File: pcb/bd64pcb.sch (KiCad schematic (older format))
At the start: 15 parts

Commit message: switch matrix & usbc prep
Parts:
- added D? (x64): SOD123, symbol Device:D_Small
- added F?: 500mA, symbol Device:Polyfuse_Small
- added J?: USB_C_Receptacle, symbol Connector:USB_C_Receptacle
- added MX? (x64): MX-NoLED, symbol MX_Alps_Hybrid:MX-NoLED
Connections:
- net labels added: VCC, col0, row0
- wire segments 43 -> 242
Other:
- moved on the sheet: C?, R?, SW?, U?, Y?

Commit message: mcp expander
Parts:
- removed D? (x24): SOD123, symbol Device:D_Small
- removed F?: 500mA, symbol Device:Polyfuse_Small
- removed J?: USB_C_Receptacle, symbol Connector:USB_C_Receptacle
- removed MX? (x24): MX-NoLED, symbol MX_Alps_Hybrid:MX-NoLED
- added C? (x4): 0.47uF, symbol Device:C_Small
- added C?: 22uF, symbol Device:CP1_Small
- added C? (x3): 0.1uF, symbol Device:C_Small
- added C?: 1uF, symbol Device:C_Small
- added D? (x25): SOD123, symbol Device:D_Small
- added F?: 500mA, symbol Device:Polyfuse_Small
- added J?: USB_C_Receptacle_USB2.0, symbol Connector:USB_C_Receptacle_USB2.0
- added JP? (x4): SolderJumper_2_Bridged, symbol Jumper:SolderJumper_2_Bridged
- added JP? (x5): SolderJumper_3_Bridged12, symbol Jumper:SolderJumper_3_Bridged12
- added MX? (x25): MX-NoLED, symbol MX_Alps_Hybrid:MX-NoLED
- added R?: 20k, symbol Device:R_Small
- added R? (x2): 5.1k, symbol Device:R_Small
- added R? (x2): 100k, symbol Device:R_Small
- added TP?: TestPoint, symbol Connector:TestPoint
- added U? (x64): QBLP677R-RGB, RGB-REVERSE_MOUNT, symbol QBLP677R-RGB:QBLP677R-RGB
- added U?: MCP23017_SO, Package_SO:SOIC-28W_7.5x17.9mm_P1.27mm, symbol Interface_Expansion:MCP23017_SO
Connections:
- net labels added: CS1, CS10, CS11, CS12, CS13, CS14, CS15, CS16, CS2, CS3, CS4, CS5, CS6, CS7, CS8, CS9, IICRST, INTB, SCL, SDA, SDB, SW1, SW10, SW11, SW12, SW2, SW3, SW4, SW5, SW6, SW7, SW8, SW9, col1, col10, col11, col12, col2, col3, col4, col5, col6, col7, col8, col9, row1, row2, row3, row4
- wire segments 242 -> 968
- no-connect marks 0 -> 8
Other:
- moved on the sheet: C?, D?, MX?, R?, SW?, U?, Y?

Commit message: numbering components
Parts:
- added F2: 500mA, symbol Device:Polyfuse_Small
- added J2: USB_B_Micro, symbol Connector:USB_B_Micro
- added R5, R6, R7: 4.7k, symbol Device:R_Small
- gave numbers to parts that had none: 236
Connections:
- net +5V: now also F2.1, R5.2, R6.2, R7.2
- net D+: now also J2.3 (D+)
- net D-: now also J2.2 (D-)
- net GND: now also J2.5 (GND), J2.6 (Shield)
- net IICRST: now also U1.29 (PB5)
- net INTB: now also U1.20 (PD2), R5.1
- net SCL: now also U1.19 (PD1), R6.1
- net SDA: now also U1.18 (PD0), R7.1
- net SDB: now also U1.31 (PC6)
- net VCC: now also F2.2, J2.1 (VBUS)
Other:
- moved on the sheet: C1, C10, C11, C12, C13, C14, C15, C16, C2, C3, C4, C5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

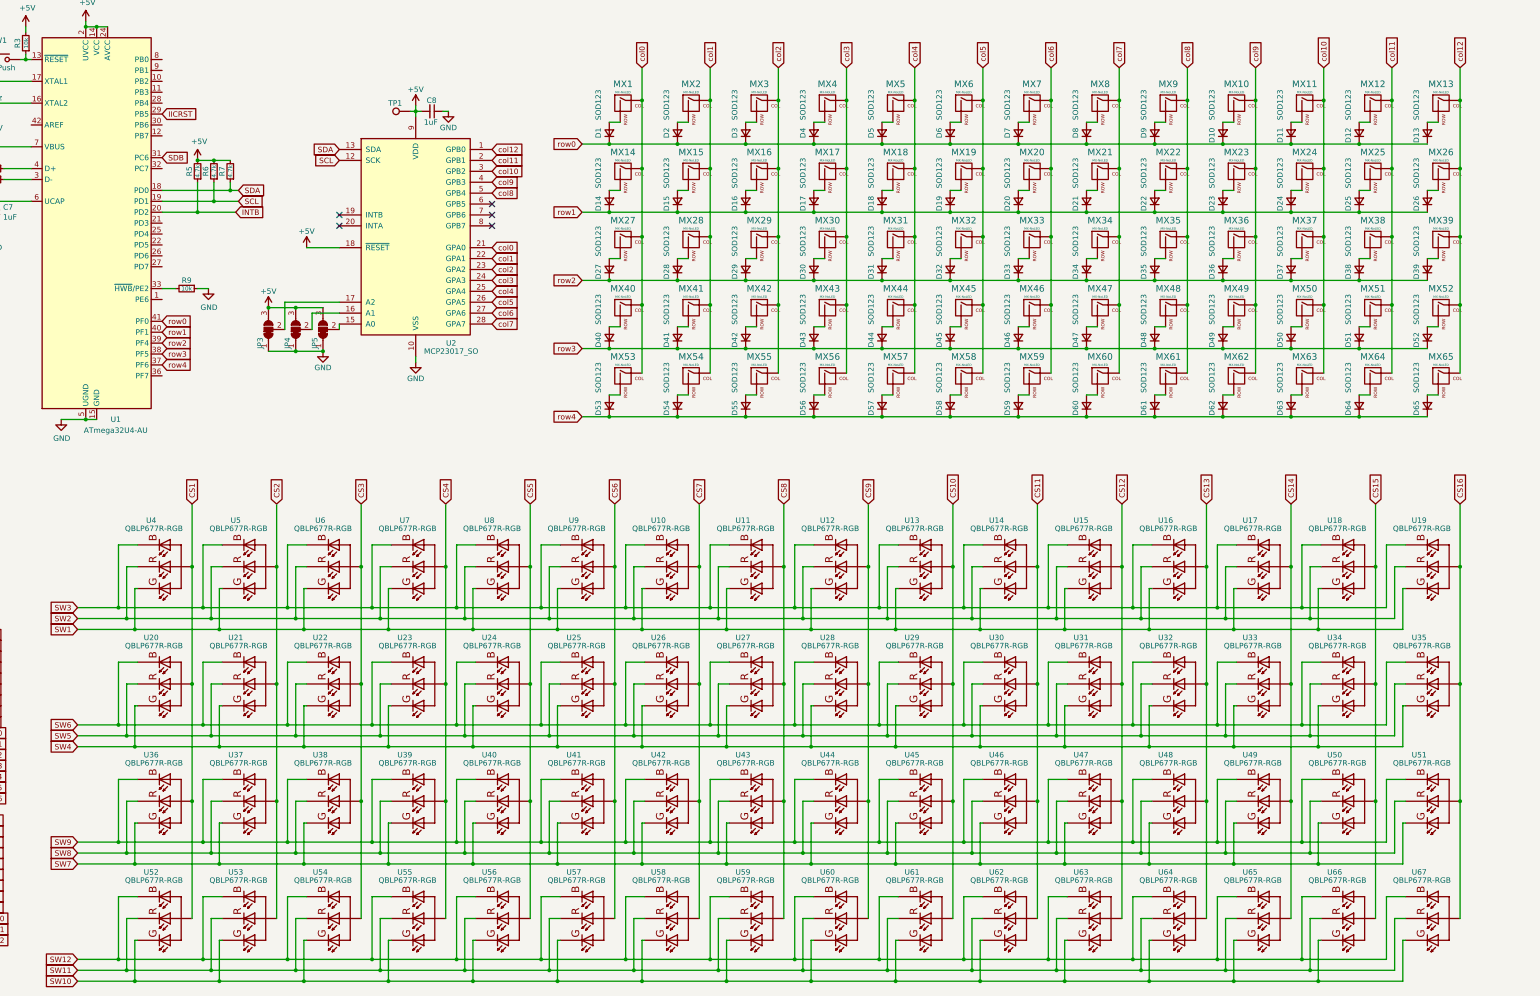
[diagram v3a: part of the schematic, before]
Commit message: assigning footprints
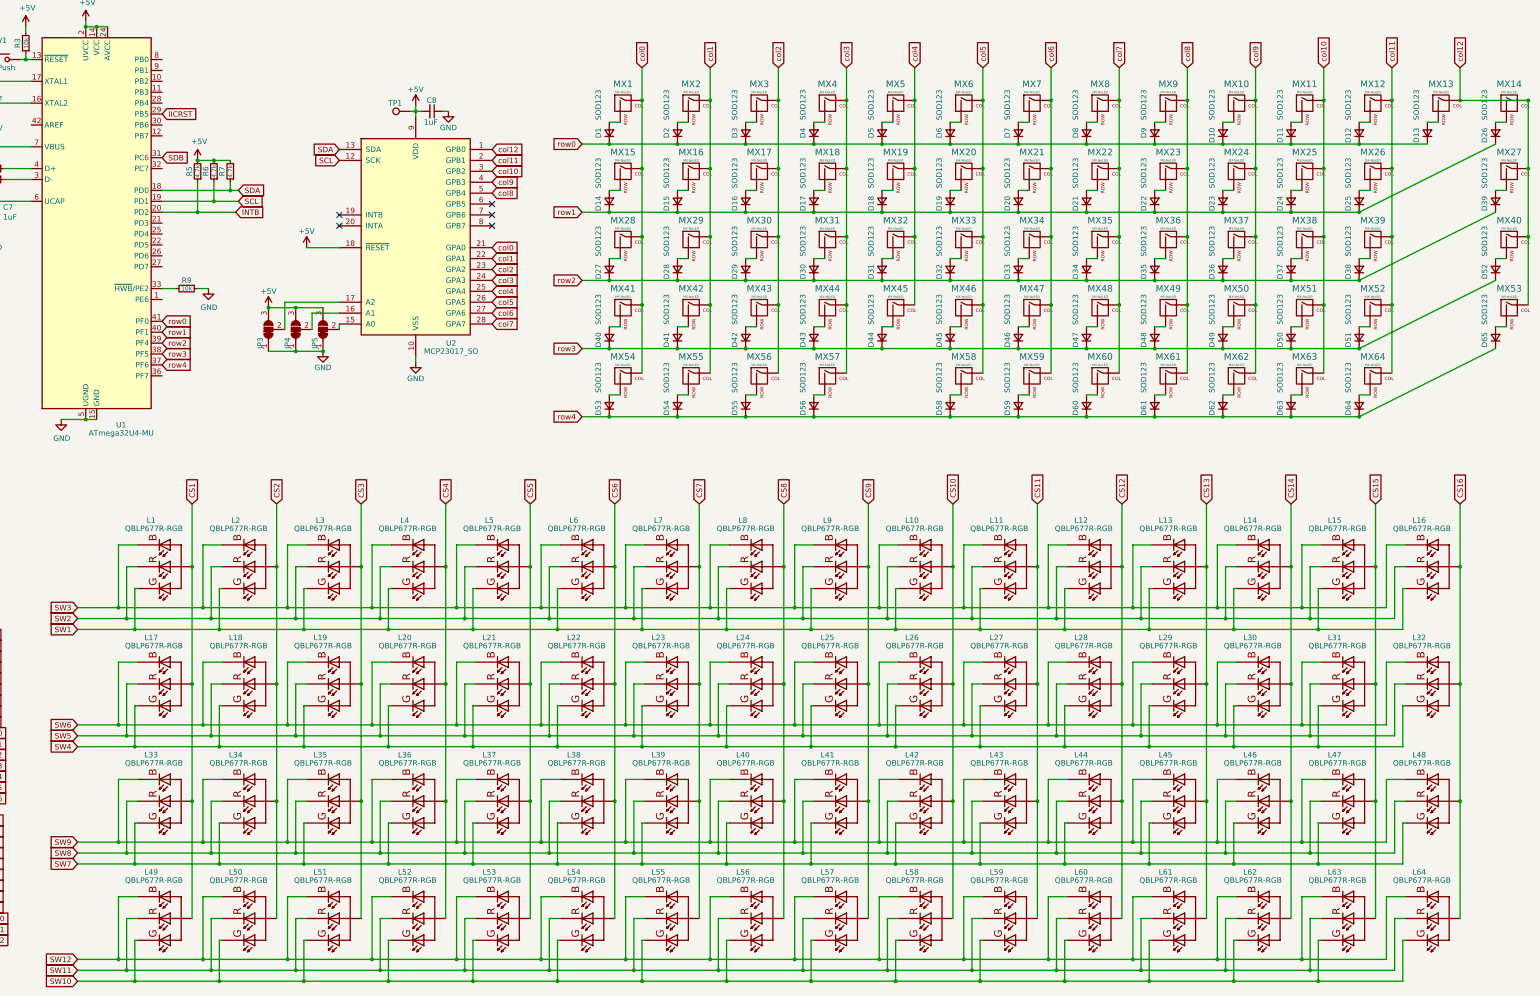
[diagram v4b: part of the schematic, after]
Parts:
- removed D57: SOD123, symbol Device:D_Small
- removed MX57: MX-NoLED, symbol MX_Alps_Hybrid:MX-NoLED
- removed U1: ATmega32U4-AU, Package_QFP:TQFP-44_10x10mm_P0.8mm, symbol MCU_Microchip_ATmega:ATmega32U4-AU
- removed U10, U11, U12, U13, U14, U15, U16, U17, U18, U19, U22, U23, U24, U25, U26, U27, U28, U29, U30, U31, U32, U33, U34, U35, U36, U37, U38, U39, U40, U41, U42, U43, U44, U45, U46, U47, U48, U49, U50, U51, U52, U53, U54, U55, U56, U57, U58, U59, U6, U60, U61, U62, U63, U64, U65, U66, U67, U7, U8, U9: QBLP677R-RGB, RGB-REVERSE_MOUNT, symbol QBLP677R-RGB:QBLP677R-RGB
- added L10, L11, L12, L13, L14, L15, L16, L19, L20, L21, L22, L23, L24, L25, L26, L27, L28, L29, L3, L30, L31, L32, L33, L34, L35, L36, L37, L38, L39, L4, L40, L41, L42, L43, L44, L45, L46, L47, L48, L49, L5, L50, L51, L52, L53, L54, L55, L56, L57, L58, L59, L6, L60, L61, L62, L63, L64, L7, L8, L9: QBLP677R-RGB, QBLP677R-RGB:RGB-REVERSE_MOUNT, symbol QBLP677R-RGB:QBLP677R-RGB
- added U1: ATmega32U4-MU, Package_DFN_QFN:QFN-44-1EP_7x7mm_P0.5mm_EP5.2x5.2mm, symbol MCU_Microchip_ATmega:ATmega32U4-MU
- C1, C10, C11, C12, C13, C14, C15, C16, C2, C3, C4, C5, C6, C7, C8, C9: footprint (none) -> Capacitor_SMD:C_0805_2012Metric
- D1, D10, D11, D12, D13, D14, D15, D16, D17, D18, D19, D2, D20, D21, D22, D23, D24, D25, D26, D27, D28, D29, D3, D30, D31, D32, D33, D34, D35, D36, D37, D38, D39, D4, D40, D41, D42, D43, D44, D45, D46, D47, D48, D49, D5, D50, D51, D52, D53, D54, D55, D56, D58, D59, D6, D60, D61, D62, D63, D64, D65, D7, D8, D9: footprint (none) -> Diode_SMD:D_SOD-123
- F1, F2: footprint (none) -> Fuse:Fuse_1206_3216Metric
- J2: footprint (none) -> random-keyboard-parts:Molex-0548190589
- L1: renamed from U4; footprint RGB-REVERSE_MOUNT -> QBLP677R-RGB:RGB-REVERSE_MOUNT
- L17: renamed from U20; footprint RGB-REVERSE_MOUNT -> QBLP677R-RGB:RGB-REVERSE_MOUNT
- L18: renamed from U21; footprint RGB-REVERSE_MOUNT -> QBLP677R-RGB:RGB-REVERSE_MOUNT
- L2: renamed from U5; footprint RGB-REVERSE_MOUNT -> QBLP677R-RGB:RGB-REVERSE_MOUNT
- MX1, MX10, MX11, MX12, MX13, MX2, MX3, MX4, MX5, MX58, MX59, MX6, MX7, MX8, MX9: footprint (none) -> MX_Alps_Hybrid:MX-1U-NoLED
- MX14: renamed from MX26; footprint (none) -> MX_Alps_Hybrid:MX-1U-NoLED
- MX15: renamed from MX14; footprint (none) -> MX_Alps_Hybrid:MX-1.25U-NoLED
- MX16: renamed from MX15; footprint (none) -> MX_Alps_Hybrid:MX-1U-NoLED
- MX17: renamed from MX16; footprint (none) -> MX_Alps_Hybrid:MX-1U-NoLED
- MX18: renamed from MX17; footprint (none) -> MX_Alps_Hybrid:MX-1U-NoLED
- MX19: renamed from MX18; footprint (none) -> MX_Alps_Hybrid:MX-1U-NoLED
- MX20: renamed from MX19; footprint (none) -> MX_Alps_Hybrid:MX-1U-NoLED
- MX21: renamed from MX20; footprint (none) -> MX_Alps_Hybrid:MX-1U-NoLED
- MX22: renamed from MX21; footprint (none) -> MX_Alps_Hybrid:MX-1U-NoLED
- MX23: renamed from MX22; footprint (none) -> MX_Alps_Hybrid:MX-1U-NoLED
- MX24: renamed from MX23; footprint (none) -> MX_Alps_Hybrid:MX-1U-NoLED
- MX25: renamed from MX24; footprint (none) -> MX_Alps_Hybrid:MX-1U-NoLED
- MX26: renamed from MX25; footprint (none) -> MX_Alps_Hybrid:MX-1U-NoLED
- MX27: renamed from MX39; footprint (none) -> MX_Alps_Hybrid:MX-1.75U-NoLED
- MX28: renamed from MX27; footprint (none) -> MX_Alps_Hybrid:MX-1.5U-NoLED
- MX29: renamed from MX28; footprint (none) -> MX_Alps_Hybrid:MX-1U-NoLED
- MX30: renamed from MX29; footprint (none) -> MX_Alps_Hybrid:MX-1U-NoLED
- MX31: renamed from MX30; footprint (none) -> MX_Alps_Hybrid:MX-1U-NoLED
- MX32: renamed from MX31; footprint (none) -> MX_Alps_Hybrid:MX-1U-NoLED
- MX33: renamed from MX32; footprint (none) -> MX_Alps_Hybrid:MX-1U-NoLED
- MX34: renamed from MX33; footprint (none) -> MX_Alps_Hybrid:MX-1U-NoLED
- MX35: renamed from MX34; footprint (none) -> MX_Alps_Hybrid:MX-1U-NoLED
- MX36: renamed from MX35; footprint (none) -> MX_Alps_Hybrid:MX-1U-NoLED
- MX37: renamed from MX36; footprint (none) -> MX_Alps_Hybrid:MX-1U-NoLED
- MX38: renamed from MX37; footprint (none) -> MX_Alps_Hybrid:MX-1U-NoLED
- MX39: renamed from MX38; footprint (none) -> MX_Alps_Hybrid:MX-1U-NoLED
- MX40: renamed from MX52; footprint (none) -> MX_Alps_Hybrid:MX-1.5U-NoLED
- MX41: renamed from MX40; footprint (none) -> MX_Alps_Hybrid:MX-1.75U-NoLED
- MX42: renamed from MX41; footprint (none) -> MX_Alps_Hybrid:MX-1U-NoLED
- MX43: renamed from MX42; footprint (none) -> MX_Alps_Hybrid:MX-1U-NoLED
- MX44: renamed from MX43; footprint (none) -> MX_Alps_Hybrid:MX-1U-NoLED
- MX45: renamed from MX44; footprint (none) -> MX_Alps_Hybrid:MX-1U-NoLED
- MX46: renamed from MX45; footprint (none) -> MX_Alps_Hybrid:MX-1U-NoLED
- MX47: renamed from MX46; footprint (none) -> MX_Alps_Hybrid:MX-1U-NoLED
- MX48: renamed from MX47; footprint (none) -> MX_Alps_Hybrid:MX-1U-NoLED
- MX49: renamed from MX48; footprint (none) -> MX_Alps_Hybrid:MX-1U-NoLED
- MX50: renamed from MX49; footprint (none) -> MX_Alps_Hybrid:MX-1U-NoLED
- MX51: renamed from MX50; footprint (none) -> MX_Alps_Hybrid:MX-1U-NoLED
- MX52: renamed from MX51; footprint (none) -> MX_Alps_Hybrid:MX-1U-NoLED
- MX53: renamed from MX65; footprint (none) -> MX_Alps_Hybrid:MX-1.25U-NoLED
- MX54: renamed from MX53; footprint (none) -> MX_Alps_Hybrid:MX-1.25U-NoLED
- MX55: renamed from MX54; footprint (none) -> MX_Alps_Hybrid:MX-1.25U-NoLED
- MX56: renamed from MX55; footprint (none) -> MX_Alps_Hybrid:MX-1.5U-NoLED
- MX57: renamed from MX56; footprint (none) -> MX_Alps_Hybrid:MX-1.5U-NoLED
- MX60: footprint (none) -> MX_Alps_Hybrid:MX-1.5U-NoLED
- MX61, MX62, MX63, MX64: footprint (none) -> MX_Alps_Hybrid:MX-1.25U-NoLED
- R1, R10, R11, R12, R2, R3, R4, R5, R6, R7, R8, R9: footprint (none) -> Resistor_SMD:R_0805_2012Metric
- TP1: footprint (none) -> TestPoint:TestPoint_Plated_Hole_D2.0mm
- Y1: footprint (none) -> Crystal:Crystal_SMD_3225-4Pin_3.2x2.5mm
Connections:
- net +5V: now also U1.14 (VCC), U1.2 (UVCC), U1.24 (AVCC), U1.34 (VCC), U1.44 (AVCC), U1.7 (VBUS)
- net CS1: now also L33.COMMON_ANODE, L49.COMMON_ANODE
- net CS10: now also L10.COMMON_ANODE, L26.COMMON_ANODE, L42.COMMON_ANODE, L58.COMMON_ANODE
- net CS11: now also L11.COMMON_ANODE, L27.COMMON_ANODE, L43.COMMON_ANODE, L59.COMMON_ANODE
- net CS12: now also L12.COMMON_ANODE, L28.COMMON_ANODE, L44.COMMON_ANODE, L60.COMMON_ANODE
- net CS13: now also L13.COMMON_ANODE, L29.COMMON_ANODE, L45.COMMON_ANODE, L61.COMMON_ANODE
- net CS14: now also L14.COMMON_ANODE, L30.COMMON_ANODE, L46.COMMON_ANODE, L62.COMMON_ANODE
- net CS15: now also L15.COMMON_ANODE, L31.COMMON_ANODE, L47.COMMON_ANODE, L63.COMMON_ANODE
- net CS16: now also L16.COMMON_ANODE, L32.COMMON_ANODE, L48.COMMON_ANODE, L64.COMMON_ANODE
- net CS2: now also L34.COMMON_ANODE, L50.COMMON_ANODE
- net CS3: now also L19.COMMON_ANODE, L3.COMMON_ANODE, L35.COMMON_ANODE, L51.COMMON_ANODE
- net CS4: now also L20.COMMON_ANODE, L36.COMMON_ANODE, L4.COMMON_ANODE, L52.COMMON_ANODE
- net CS5: now also L21.COMMON_ANODE, L37.COMMON_ANODE, L5.COMMON_ANODE, L53.COMMON_ANODE
- net CS6: now also L22.COMMON_ANODE, L38.COMMON_ANODE, L54.COMMON_ANODE, L6.COMMON_ANODE
- net CS7: now also L23.COMMON_ANODE, L39.COMMON_ANODE, L55.COMMON_ANODE, L7.COMMON_ANODE
- net CS8: now also L24.COMMON_ANODE, L40.COMMON_ANODE, L56.COMMON_ANODE, L8.COMMON_ANODE
- net CS9: now also L25.COMMON_ANODE, L41.COMMON_ANODE, L57.COMMON_ANODE, L9.COMMON_ANODE
- net GND: now also U1.15 (GND), U1.23 (GND), U1.35 (GND), U1.43 (GND), U1.45 (GND), U1.5 (UGND)
- net IICRST: now also U1.29 (PB5)
- net INTB: now also U1.20 (PD2)
- net SCL: now also U1.19 (PD1)
- net SDA: now also U1.18 (PD0)
- net SDB: now also U1.31 (PC6)
- net SW1: now also L10.2, L11.2, L12.2, L13.2, L14.2, L15.2, L16.2, L3.2, L4.2, L5.2, L6.2, L7.2, L8.2, L9.2
- net SW10: now also L49.2, L50.2, L51.2, L52.2, L53.2, L54.2, L55.2, L56.2, L57.2, L58.2, L59.2, L60.2, L61.2, L62.2, L63.2, L64.2
- net SW11: now also L49.3, L50.3, L51.3, L52.3, L53.3, L54.3, L55.3, L56.3, L57.3, L58.3, L59.3, L60.3, L61.3, L62.3, L63.3, L64.3
- net SW12: now also L49.1, L50.1, L51.1, L52.1, L53.1, L54.1, L55.1, L56.1, L57.1, L58.1, L59.1, L60.1, L61.1, L62.1, L63.1, L64.1
- net SW2: now also L10.3, L11.3, L12.3, L13.3, L14.3, L15.3, L16.3, L3.3, L4.3, L5.3, L6.3, L7.3, L8.3, L9.3
- net SW3: now also L10.1, L11.1, L12.1, L13.1, L14.1, L15.1, L16.1, L3.1, L4.1, L5.1, L6.1, L7.1, L8.1, L9.1
- net SW4: now also L19.2, L20.2, L21.2, L22.2, L23.2, L24.2, L25.2, L26.2, L27.2, L28.2, L29.2, L30.2, L31.2, L32.2
- net SW5: now also L19.3, L20.3, L21.3, L22.3, L23.3, L24.3, L25.3, L26.3, L27.3, L28.3, L29.3, L30.3, L31.3, L32.3
- net SW6: now also L19.1, L20.1, L21.1, L22.1, L23.1, L24.1, L25.1, L26.1, L27.1, L28.1, L29.1, L30.1, L31.1, L32.1
- net SW7: now also L33.2, L34.2, L35.2, L36.2, L37.2, L38.2, L39.2, L40.2, L41.2, L42.2, L43.2, L44.2, L45.2, L46.2, L47.2, L48.2
- net SW8: now also L33.3, L34.3, L35.3, L36.3, L37.3, L38.3, L39.3, L40.3, L41.3, L42.3, L43.3, L44.3, L45.3, L46.3, L47.3, L48.3
- net SW9: now also L33.1, L34.1, L35.1, L36.1, L37.1, L38.1, L39.1, L40.1, L41.1, L42.1, L43.1, L44.1, L45.1, L46.1, L47.1, L48.1
- net row0: now also U1.41 (PF0)
- net row1: now also U1.40 (PF1)
- net row2: now also U1.39 (PF4)
- net row3: now also U1.38 (PF5)
- net row4: now also U1.37 (PF6)
- net at R3.1, SW1.2: now also U1.13 (~RESET)
- net at C6.2, Y1.2: now also U1.16 (XTAL2)
- net at C5.2, Y1.4: now also U1.17 (XTAL1)
- net at R8.1: now also U1.3 (D-)
- net at R9.2: now also U1.33 (~HWB~/PE2)
- net at R4.1: now also U1.4 (D+)
- net at C7.1: now also U1.6 (UCAP)
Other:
- moved on the sheet: D26, D39, D52, D65, MX14, MX27, MX40, MX53

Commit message: switches placed
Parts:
- J1: footprint (none) -> Connector_USB:USB_C_Receptacle_GCT_USB4085
- JP1, JP2, JP6, JP7: footprint (none) -> Jumper:SolderJumper-2_P1.3mm_Bridged_RoundedPad1.0x1.5mm
- JP3, JP4, JP5, JP8, JP9: footprint (none) -> Jumper:SolderJumper-3_P1.3mm_Bridged12_RoundedPad1.0x1.5mm
- SW1: footprint (none) -> random-keyboard-parts:SKQG-1155865
- renumbered D26 to D14, D14 to D15, D15 to D16, D16 to D17, D17 to D18, D18 to D19, D19 to D20, D20 to D21, D21 to D22, D22 to D23, D23 to D24, D24 to D25, D25 to D26, D39 to D27, D27 to D28, D28 to D29, D29 to D30, D30 to D31, D31 to D32, D32 to D33, D33 to D34, D34 to D35, D35 to D36, D36 to D37, D37 to D38, D38 to D39, D52 to D40, D40 to D41, D41 to D42, D42 to D43, D43 to D44, D44 to D45, D45 to D46, D46 to D47, D47 to D48, D48 to D49, D49 to D50, D50 to D51, D51 to D52, D65 to D53, D53 to D54, D54 to D55, D55 to D56, D56 to D57
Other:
- moved on the sheet: C10, C11, C12, C13, C14, C15, C16, C8, C9, D1, D10, D11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

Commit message: LEDS place (poorly) and MCP footprint changed to QFN
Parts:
- removed U2: MCP23017_SO, Package_SO:SOIC-28W_7.5x17.9mm_P1.27mm, symbol Interface_Expansion:MCP23017_SO
- added U2: MCP23017_ML, Package_DFN_QFN:QFN-28-1EP_6x6mm_P0.65mm_EP4.25x4.25mm, symbol Interface_Expansion:MCP23017_ML
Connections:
- net +5V: now also U2.14 (~RESET~), U2.5 (VDD)
- net GND: now also U2.29 (EP), U2.6 (VSS)
- net SCL: now also U2.8 (SCK)
- net SDA: now also U2.9 (SDA)
- net col0: now also U2.17 (GPA0)
- net col1: now also U2.18 (GPA1)
- net col10: now also U2.27 (GPB2)
- net col11: now also U2.26 (GPB1)
- net col12: now also U2.25 (GPB0)
- net col2: now also U2.19 (GPA2)
- net col3: now also U2.20 (GPA3)
- net col4: now also U2.21 (GPA4)
- net col5: now also U2.22 (GPA5)
- net col6: now also U2.23 (GPA6)
- net col7: now also U2.24 (GPA7)
- net col8: now also U2.1 (GPB4)
- net col9: now also U2.28 (GPB3)
- net at JP5.2 (C): now also U2.11 (A0)
- net at JP4.2 (C): now also U2.12 (A1)
- net at JP3.2 (C): now also U2.13 (A2)
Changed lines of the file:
@@
 	1    0    0    -1
 $EndComp
-$Comp
-L Interface_Expansion:MCP23017_SO U2
-U 1 1 71ED41B4
-P 7300 3225
-F 0 "U2" H 7625 2250 50  0000 C CNN
-F 1 "MCP23017_SO" H 7625 2175 50  0000 C CNN
-F 2 "Package_SO:SOIC-28W_7.5x17.9mm_P1.27mm" H 7500 2225 50  0001 L CNN
-F 3 "http://ww1.microchip.com/downloads/en/DeviceDoc/20001952C.pdf" H 7500 2125 50  0001 L CNN
-	1    7300 3225
-	1    0    0    -1
-$EndComp
 Text GLabel 6600 2525 0    50   Input ~ 0
 SCL
@@
 Connection ~ 17500 3225
 Connection ~ 17500 2600
+$Comp
+L Interface_Expansion:MCP23017_ML U2
+U 1 1 63AD17B8
+P 7300 3225
+F 0 "U2" H 7600 2225 50  0000 C CNN
+F 1 "MCP23017_ML" H 7625 2150 50  0000 C CNN
+F 2 "Package_DFN_QFN:QFN-28-1EP_6x6mm_P0.65mm_EP4.25x4.25mm" H 7500 2225 50  0001 L CNN
+F 3 "http://ww1.microchip.com/downloads/en/DeviceDoc/20001952C.pdf" H 7500 2125 50  0001 L CNN
+	1    7300 3225
+	1    0    0    -1
+$EndComp
+Wire Wire Line
+	7200 4325 7300 4325
+Connection ~ 7300 4325
 $EndSCHEMATC

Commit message: no good traces yet
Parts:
- MX1: footprint MX_Alps_Hybrid:MX-1U-NoLED -> MX_Only:MXOnly-1U-NoLED
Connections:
- net col0: no longer U2.17 (GPA0)
- net col1: no longer U2.18 (GPA1)
- net col10: no longer U2.27 (GPB2)
- net col11: no longer U2.26 (GPB1)
- net col12: no longer U2.25 (GPB0)
- net col2: no longer U2.19 (GPA2)
- net col3: no longer U2.20 (GPA3)
- net col4: no longer U2.21 (GPA4)
- net col5: no longer U2.22 (GPA5)
- net col6: no longer U2.23 (GPA6)
- net col7: no longer U2.24 (GPA7)
- net col8: no longer U2.1 (GPB4)
- net col9: no longer U2.28 (GPB3)
- net row0: no longer U1.41 (PF0)
- net row1: no longer U1.40 (PF1)
- net row2: no longer U1.39 (PF4)
- net row3: no longer U1.38 (PF5)
- net row4: no longer U1.37 (PF6)
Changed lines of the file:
@@
 	0    1    1    0
 $EndComp
-Text GLabel 4850 4000 2    50   Input ~ 0
+Text GLabel 4900 4000 2    50   Input ~ 0
 row0
-Text GLabel 4850 4100 2    50   Input ~ 0
+Text GLabel 4900 4100 2    50   Input ~ 0
 row1
-Text GLabel 4850 4200 2    50   Input ~ 0
+Text GLabel 4900 4200 2    50   Input ~ 0
 row2
-Text GLabel 4850 4300 2    50   Input ~ 0
+Text GLabel 4900 4300 2    50   Input ~ 0
 row3
-Text GLabel 4850 4400 2    50   Input ~ 0
+Text GLabel 4900 4400 2    50   Input ~ 0
 row4
 Text GLabel 4525 6750 0    50   Input ~ 0
@@
 SDA
 NoConn ~ 6600 3125
-Text GLabel 8000 3325 2    50   Input ~ 0
+Text GLabel 8050 3325 2    50   Input ~ 0
 col0
-Text GLabel 8000 3425 2    50   Input ~ 0
+Text GLabel 8050 3425 2    50   Input ~ 0
 col1
-Text GLabel 8000 3525 2    50   Input ~ 0
+Text GLabel 8050 3525 2    50   Input ~ 0
 col2
-Text GLabel 8000 3625 2    50   Input ~ 0
+Text GLabel 8050 3625 2    50   Input ~ 0
 col3
-Text GLabel 8000 3725 2    50   Input ~ 0
+Text GLabel 8050 3725 2    50   Input ~ 0
 col4
-Text GLabel 8000 3825 2    50   Input ~ 0
+Text GLabel 8050 3825 2    50   Input ~ 0
 col5
-Text GLabel 8000 3925 2    50   Input ~ 0
+Text GLabel 8050 3925 2    50   Input ~ 0
 col6
-Text GLabel 8000 4025 2    50   Input ~ 0
+Text GLabel 8050 4025 2    50   Input ~ 0
 col7
-Text GLabel 8000 2825 2    50   Input ~ 0
+Text GLabel 8050 2825 2    50   Input ~ 0
 col8
-Text GLabel 8000 2725 2    50   Input ~ 0
+Text GLabel 8050 2725 2    50   Input ~ 0
 col9
-Text GLabel 8000 2625 2    50   Input ~ 0
+Text GLabel 8050 2625 2    50   Input ~ 0
 col10
-Text GLabel 8000 2525 2    50   Input ~ 0
+Text GLabel 8050 2525 2    50   Input ~ 0
 col11
-Text GLabel 8000 2425 2    50   Input ~ 0
+Text GLabel 8050 2425 2    50   Input ~ 0
 col12
 $Comp
@@
 F 0 "MX1" H 9200 2225 60  0000 C CNN
 F 1 "MX-NoLED" H 9200 2150 20  0000 C CNN
-F 2 "MX_Alps_Hybrid:MX-1U-NoLED" H 8600 2000 60  0001 C CNN
+F 2 "MX_Only:MXOnly-1U-NoLED" H 8600 2000 60  0001 C CNN
 F 3 "" H 8600 2000 60  0001 C CNN
 	1    9225 2025

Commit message: boring switch traces
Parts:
- MX2, MX3: footprint MX_Alps_Hybrid:MX-1U-NoLED -> MX_Only:MXOnly-1U-NoLED
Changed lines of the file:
@@
 F 0 "MX3" H 10450 2225 60  0000 C CNN
 F 1 "MX-NoLED" H 10450 2150 20  0000 C CNN
-F 2 "MX_Alps_Hybrid:MX-1U-NoLED" H 9850 2000 60  0001 C CNN
+F 2 "MX_Only:MXOnly-1U-NoLED" H 9850 2000 60  0001 C CNN
 F 3 "" H 9850 2000 60  0001 C CNN
 	1    10475 2025
@@
 F 0 "MX2" H 9825 2225 60  0000 C CNN
 F 1 "MX-NoLED" H 9825 2150 20  0000 C CNN
-F 2 "MX_Alps_Hybrid:MX-1U-NoLED" H 9225 2000 60  0001 C CNN
+F 2 "MX_Only:MXOnly-1U-NoLED" H 9225 2000 60  0001 C CNN
 F 3 "" H 9225 2000 60  0001 C CNN
 	1    9850 2025
